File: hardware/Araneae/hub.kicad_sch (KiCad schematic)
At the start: 15 parts, among them U22 USB2514B_M2, Y3 24MHz

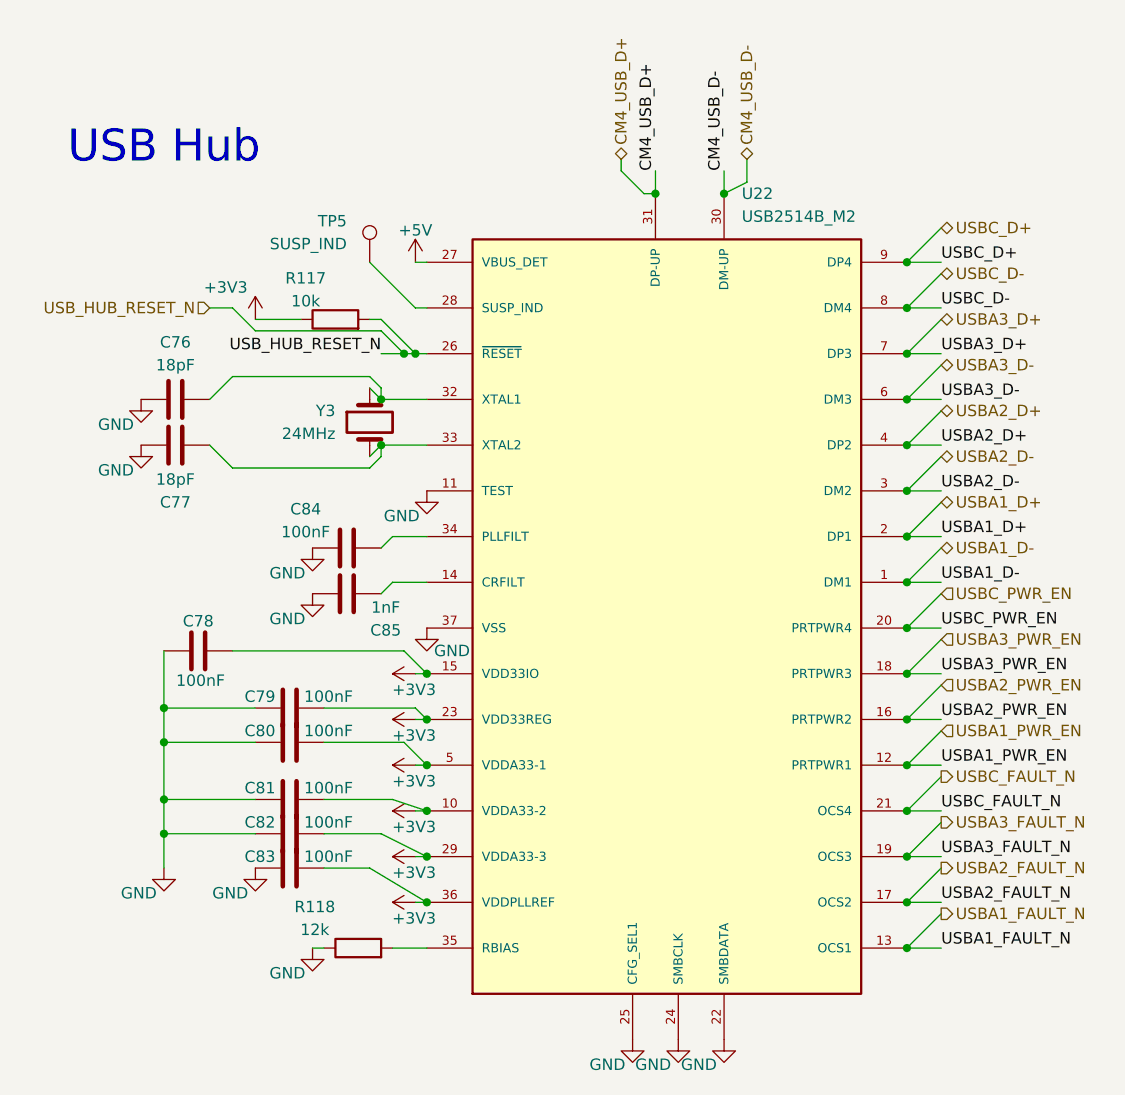
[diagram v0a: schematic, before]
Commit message: Add CI workflow for PCB checks and artifact generation
- Created a GitHub Actions workflow (`ci.yml`) to automate hardware checks including ERC, DRC, and plot generation for KiCad projects.
- Added a new footprint for the SON50P200X200X80-9N component in `SON50P200X200X80-9N.kicad_mod`.
- Introduced a new symbol for the TPS22965DSGR component in `TPS22965DSGR.kicad_sym`.
- Added a configuration file `kibot.yaml` for generating fabrication files and other outputs.
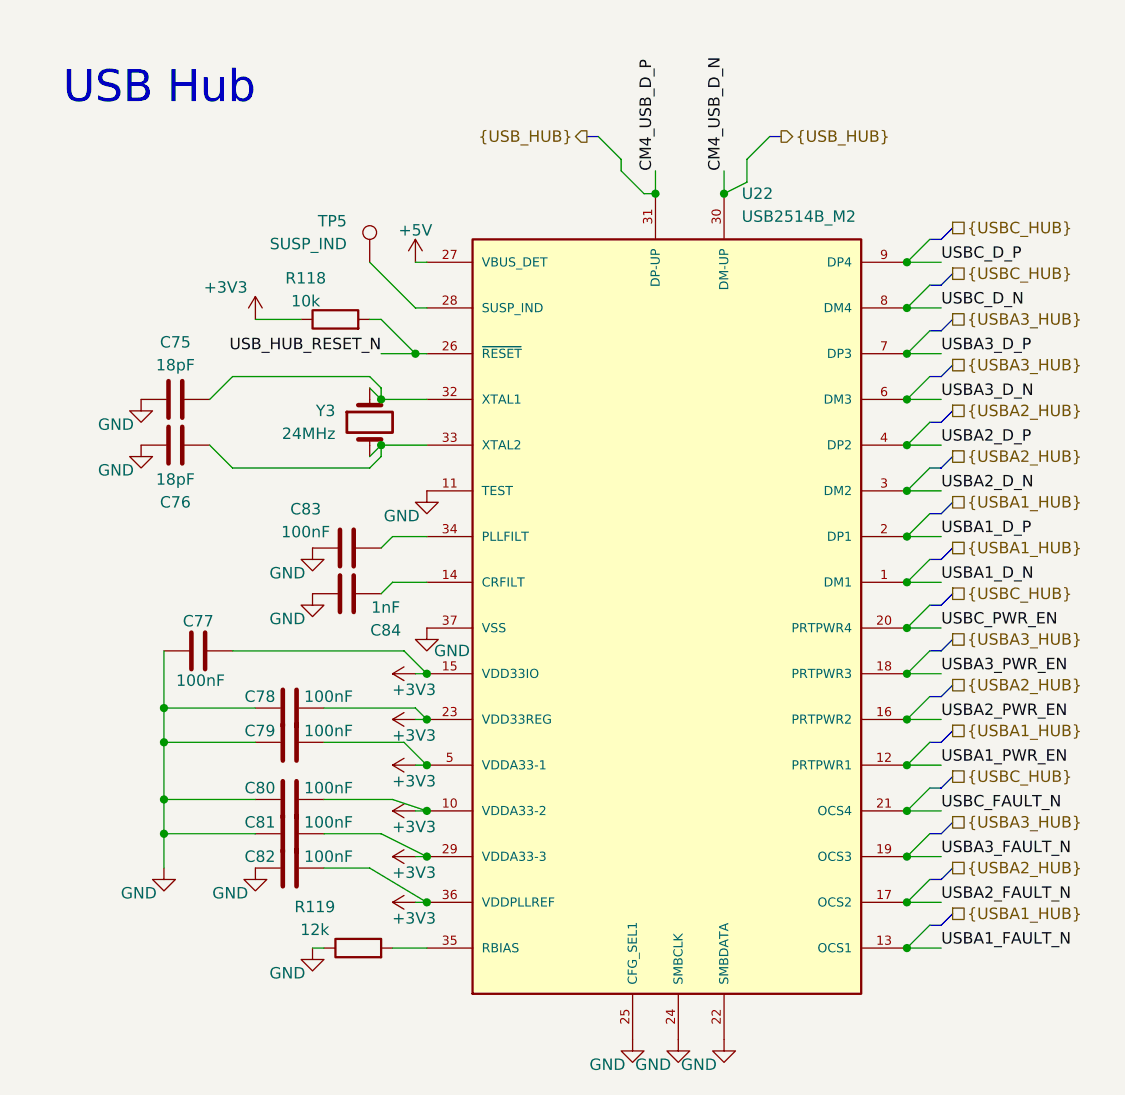
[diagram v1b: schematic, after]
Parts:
- C75: renamed from C76; footprint (none) -> Capacitor_SMD:C_0603_1608Metric
- C76: renamed from C77; footprint (none) -> Capacitor_SMD:C_0603_1608Metric
- C77: renamed from C78; footprint (none) -> Capacitor_SMD:C_0603_1608Metric
- C78: renamed from C79; footprint (none) -> Capacitor_SMD:C_0603_1608Metric
- C79: renamed from C80; footprint (none) -> Capacitor_SMD:C_0603_1608Metric
- C80: renamed from C81; footprint (none) -> Capacitor_SMD:C_0603_1608Metric
- C81: renamed from C82; footprint (none) -> Capacitor_SMD:C_0603_1608Metric
- C82: renamed from C83; footprint (none) -> Capacitor_SMD:C_0603_1608Metric
- C83: renamed from C84; footprint (none) -> Capacitor_SMD:C_0603_1608Metric
- C84: renamed from C85; footprint (none) -> Capacitor_SMD:C_0603_1608Metric
- R118: renamed from R117; footprint (none) -> Resistor_SMD:R_0603_1608Metric
- R119: renamed from R118; footprint (none) -> Resistor_SMD:R_0603_1608Metric
- TP5: footprint (none) -> TestPoint:TestPoint_Pad_D1.5mm
- U22: footprint USB2514B_M2:36-SQFN-EXPOSED-PAD -> OPL:36-SQFN-EXPOSED-PAD
- Y3: footprint (none) -> Crystal:Crystal_SMD_3225-4Pin_3.2x2.5mm
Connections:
- net CM4_USB_D+ renamed CM4_USB_D_P
- net CM4_USB_D- renamed CM4_USB_D_N
- net USBA1_D+ renamed USBA1_D_P
- net USBA1_D- renamed USBA1_D_N
- net USBA2_D+ renamed USBA2_D_P
- net USBA2_D- renamed USBA2_D_N
- net USBA3_D+ renamed USBA3_D_P
- net USBA3_D- renamed USBA3_D_N
- net USBC_D+ renamed USBC_D_P
- net USBC_D- renamed USBC_D_N
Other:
- company: (none) -> Matheus Henrique(Aka: TheusHen)
- title: (none) -> Araneae
